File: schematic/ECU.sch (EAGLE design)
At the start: 29 parts, among them J1 Break, J2 COMM, J3 PWR, J4 DISPLAY, J5 THROTTLE, J6 LED, J7 SPEED, Q1 NMOSFETSOT23, Q2 NMOSFETSOT23, Q4 PMOSFET_BSS84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

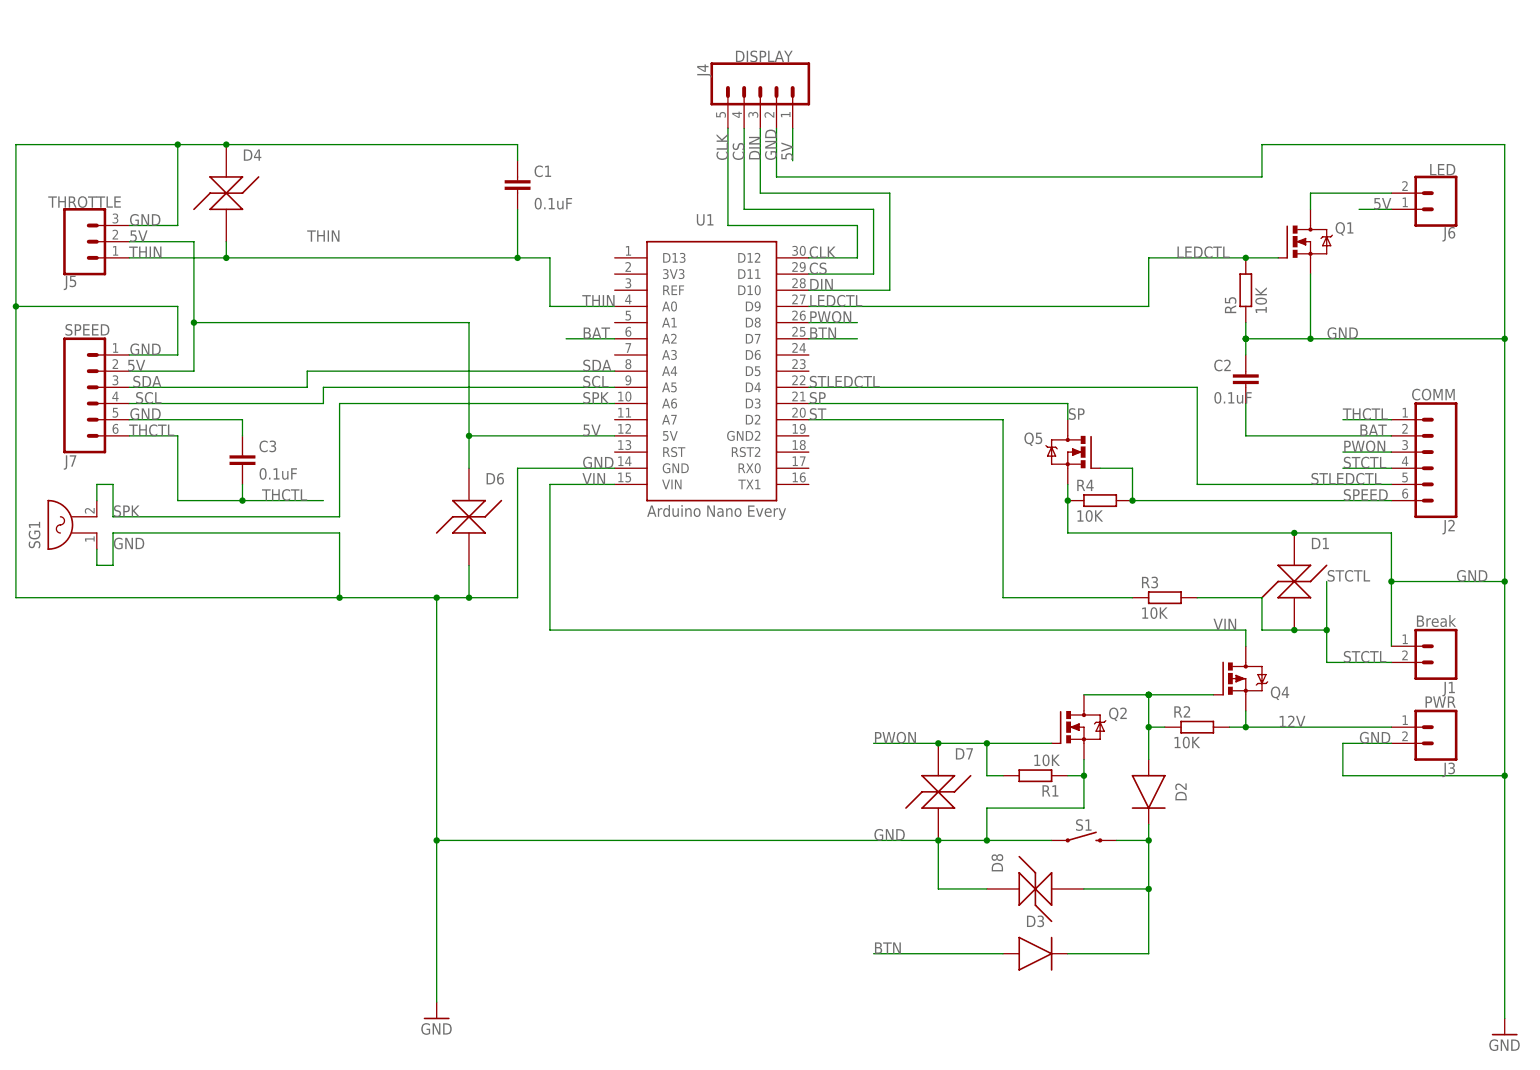
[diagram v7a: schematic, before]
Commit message: Invert stop pin logic according to new schematics
- Invert stop pin logic to use high-side p-mosfet switch
- Update TVS diode symbol
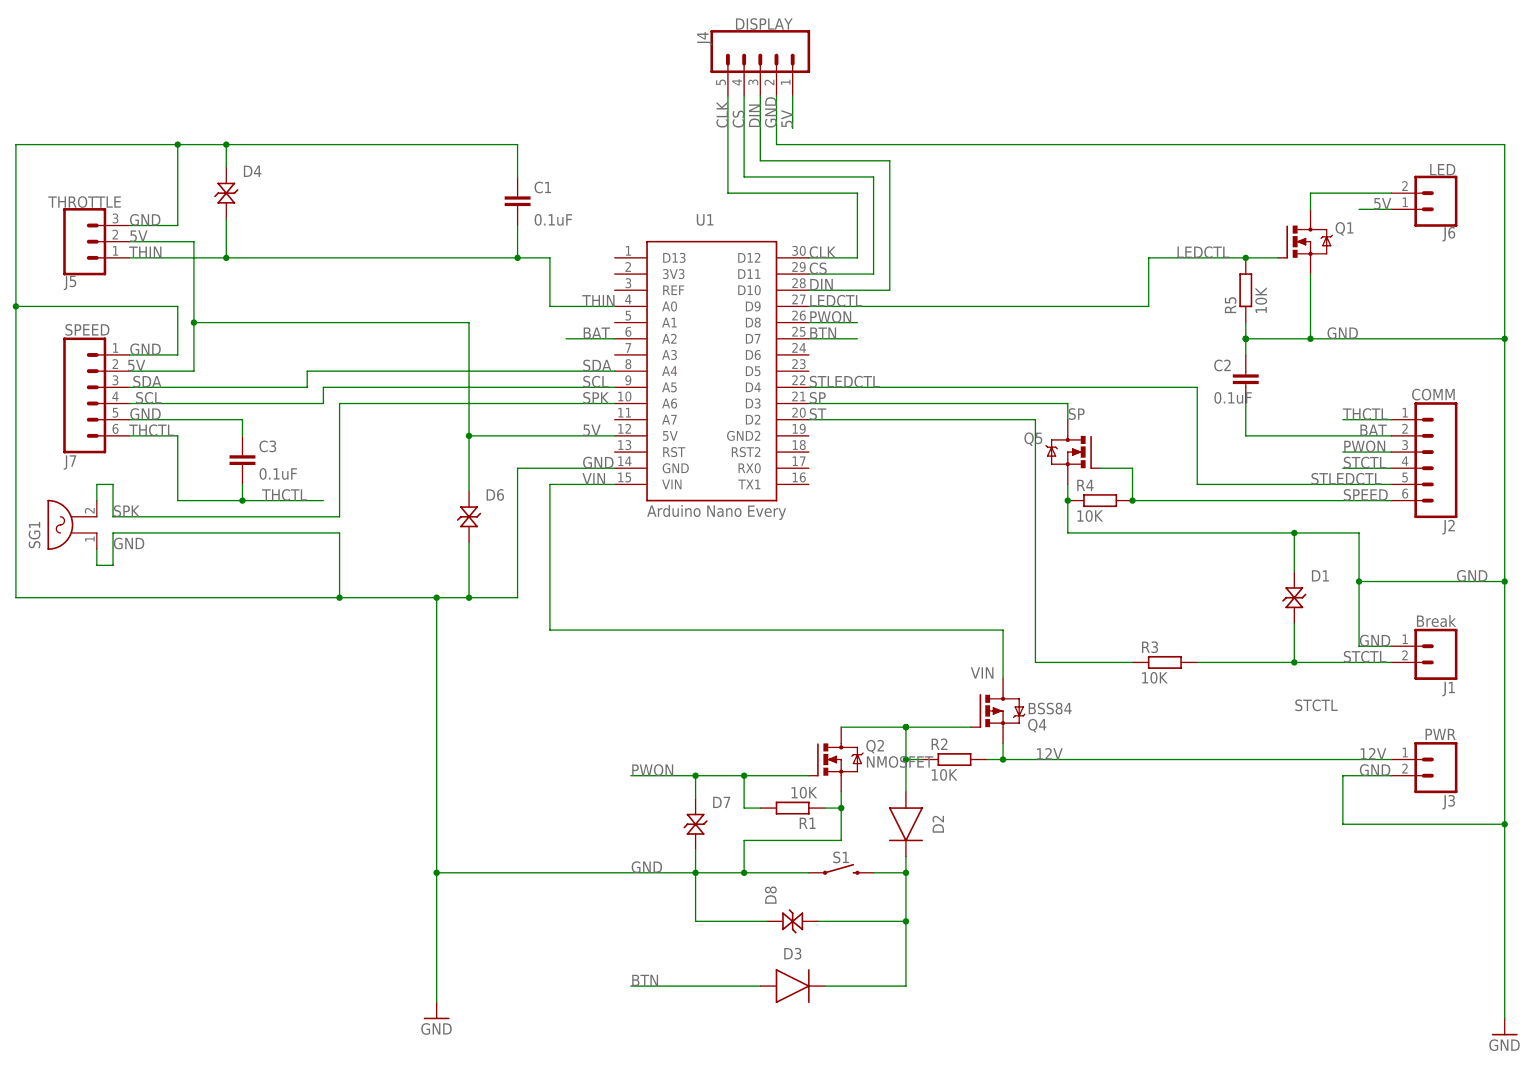
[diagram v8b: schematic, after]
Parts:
- Q1, Q2, Q5: value NMOSFETSOT23 -> NMOSFET
- Q4: value PMOSFET_BSS84 -> BSS84
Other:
- moved on the sheet: C1, D1, D2, D3, D7, D8, J3, J4, Q2, Q4, R1, R2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
